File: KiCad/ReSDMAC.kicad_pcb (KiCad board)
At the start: 4 copper layers, 38 x 38 mm, 36 parts, among them U1 10M02SCU169C8G, U2 LM1117-3.3, U3 SN74CBTD16210, U4 SN74CBTD16210, U5 SN74CBTD16210, U6 SN74CBTD16210, U7 PLCC_84_plug, U8 Super_DMAC_socket

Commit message: Production files
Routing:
- added copper zone on In2.Cu, net 3V3
- added copper zone on In1.Cu, net GND
- added copper zone on In2.Cu, net VCC
- removed copper zone on VCC.Cu, net 3V3
- removed copper zone on GND.Cu, net GND
- removed copper zone on VCC.Cu, net VCC
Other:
- net class Default removed

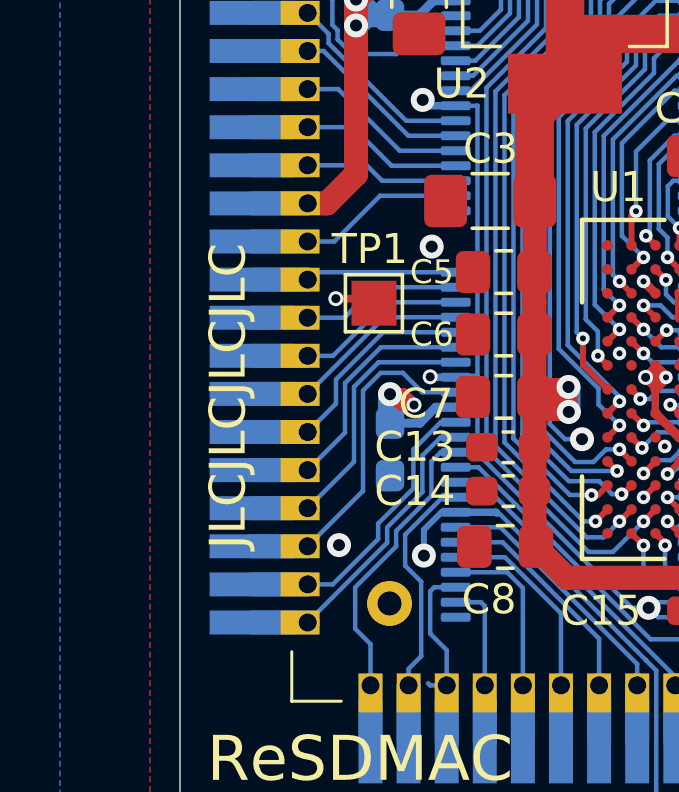
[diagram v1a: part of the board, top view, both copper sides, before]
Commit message: Added JLC production files w/ 10M04 Added pof for 0.9
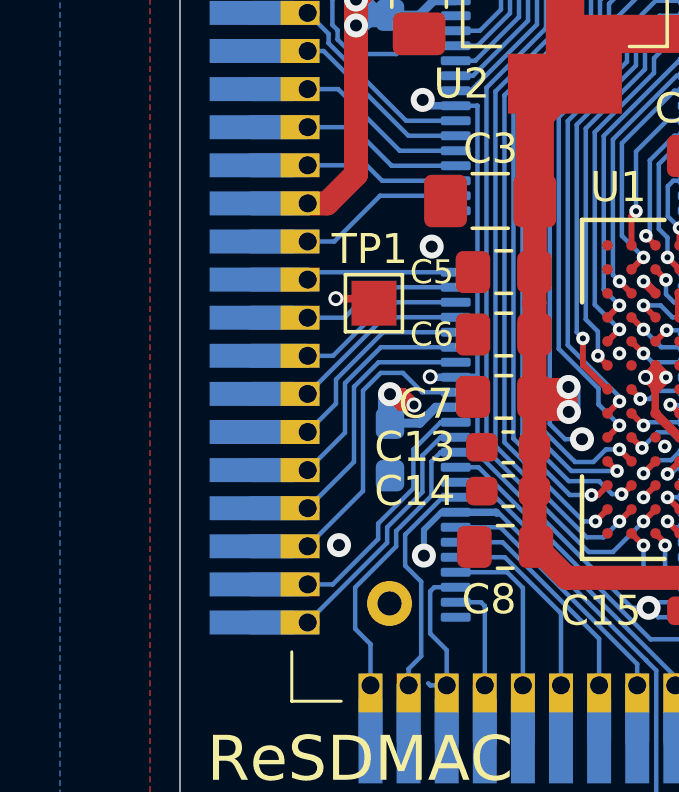
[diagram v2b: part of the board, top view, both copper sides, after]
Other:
- board text removed: "JLCJLCJLCJLC"
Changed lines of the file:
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@@
-		)
-	)
-	(gr_text "JLCJLCJLCJLC"
-		(at 126.99752 79.6026 90)
-		(layer "F.SilkS")
-		(effects
-			(font
-				(size 1.2 1.2)
-				(thickness 0.2)
-			)
 		)
 	)
